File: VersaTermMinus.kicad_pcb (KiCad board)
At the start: 2 copper layers, 83.5 x 77.7 mm, 55 parts, among them CN1 HDMI_A, CN2 DE15_Socket, CN3 USB_B_Micro, CN5 USB_B_Micro, CN6 Mini-DIN-6, CN7 TTL Serial, CN8 DE9 Socket, J2 USBDATA, Q1 2N7002, Q2 2N7002, Q3 2N7002, Q4 2N7002, Q5 2N7002, Q6 2N7002, Q7 2N7002, SW1 RESET, SW2 DEFAULTS, SW3 3V3/5V, U1 Raspberry Pi Pico, U3 MAX3232

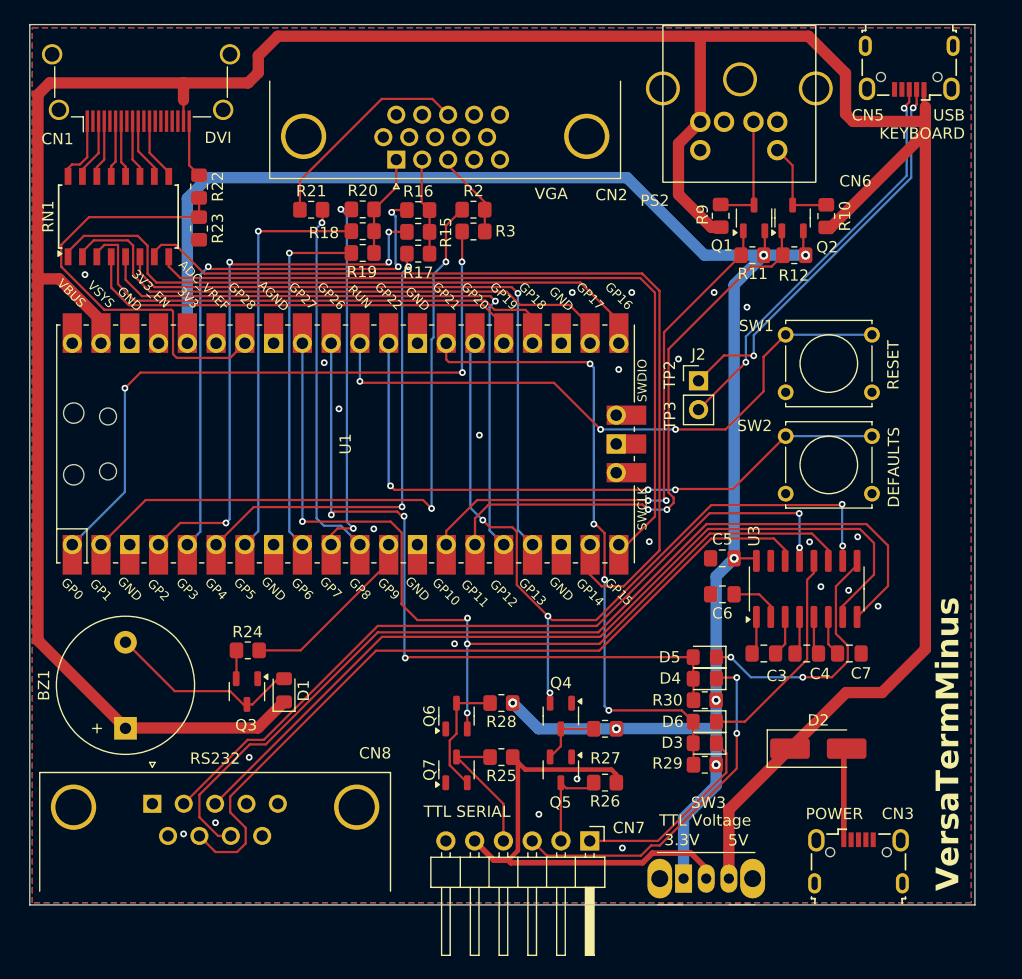
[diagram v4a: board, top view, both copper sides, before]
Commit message: fix incorrect schema symbols for 2n7002 transistors
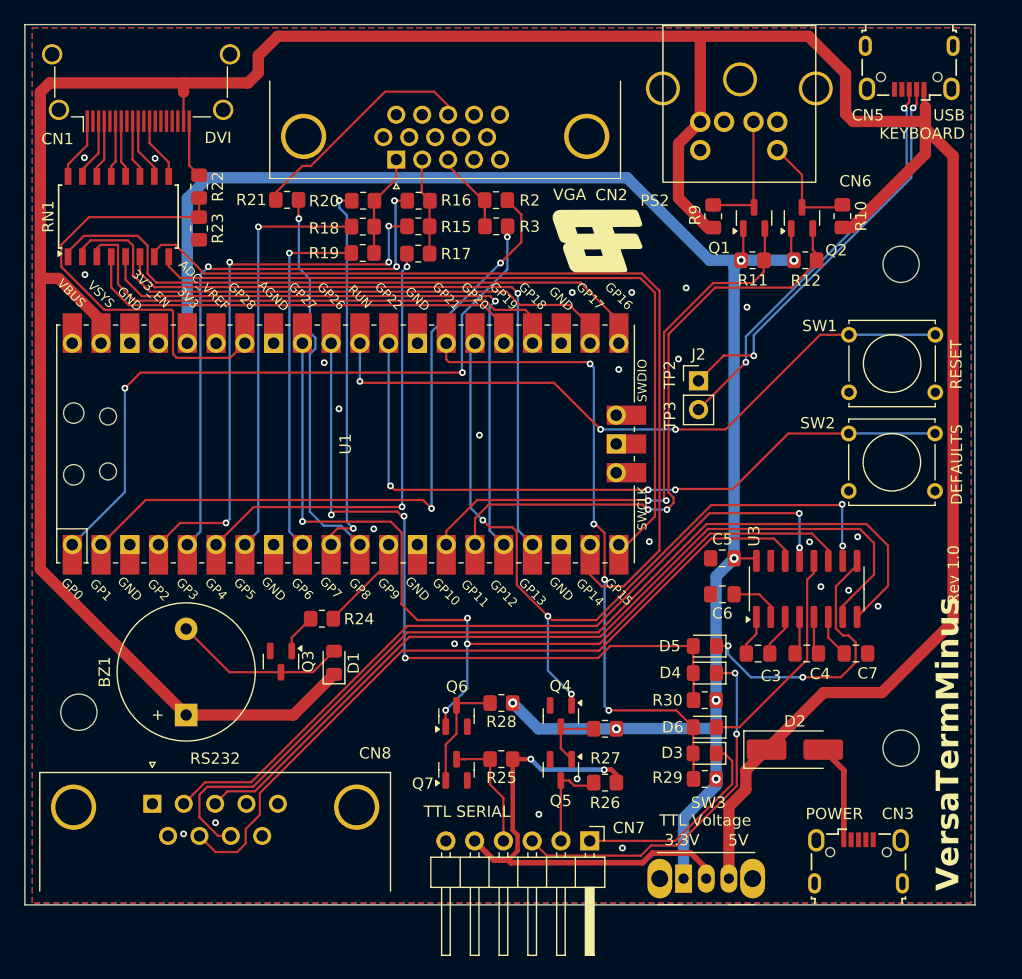
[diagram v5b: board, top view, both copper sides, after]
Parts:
- added G***: LOGO, Logos:BF, F.Cu at (108.3, 68.7)
- added G***: LOGO, Logos:tbs_logo, B.Cu at (123.7, 84.9)
- added G***: LOGO, Logos:mfmi_logo, B.Cu at (101.3, 88.3)
- added H1: MountingHole, MountingHole:MountingHole_3.2mm_M3, F.Cu at (135.1, 70.7)
- added H2: MountingHole, MountingHole:MountingHole_3.2mm_M3, F.Cu at (135.1, 113.4)
- added H3: MountingHole, MountingHole:MountingHole_3.2mm_M3, F.Cu at (62.5, 110.3)
- Q1, Q2, Q3, Q4, Q5, Q6, Q7: footprint Package_TO_SOT_SMD:SOT-23-3 -> Package_TO_SOT_SMD:SOT-23
- moved R24 7.12 mm to (84.0, 102.0)
- moved SW1 5.59 mm to (130.5, 76.9)
- moved SW2 5.57 mm to (130.5, 85.6)
- moved BZ1 5.49 mm to (72.0, 110.5)
- moved D1 5.04 mm to (85.1, 105.9)
- moved Q3 4.00 mm to (80.4, 105.8)
- moved R21 2.30 mm to (80.9, 65.0)
- moved R2 2.16 mm to (99.4, 65.0), turned to 180 degrees
- moved D2 2.07 mm to (125.8, 113.6)
- moved R3 2.07 mm to (99.4, 67.4), turned to 180 degrees
- moved R10 1.42 mm to (129.9, 66.5)
- moved R29 1.25 mm to (117.8, 116.2)
- moved R12 1.07 mm to (126.7, 70.4), turned to 180 degrees
- moved D5 0.98 mm to (117.8, 104.4)
- moved D3 0.89 mm to (117.8, 113.9)
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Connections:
- net Net-(CN2-Pad1) renamed /Red
- net Net-(CN2-Pad13) renamed /Sync
- net Net-(CN2-Pad2) renamed /Green
- net Net-(CN2-Pad3) renamed /Blue
- net Net-(Q1-D) renamed /Data
- net Net-(Q2-D) renamed /Clock
- Q1 pad 1: PS2DATA -> +3.3V
- Q1 pad 2: +3.3V -> PS2DATA
- Q2 pad 1: PS2CLK -> +3.3V
- Q2 pad 2: +3.3V -> PS2CLK
- Q3 pad 1: GND -> Net-(Q3-G)
- Q3 pad 2: Net-(Q3-G) -> GND
- Q4 pad 1: GND -> TXO
- Q4 pad 2: TXO -> GND
- Q5 pad 1: GND -> Net-(Q4-D)
- Q5 pad 2: Net-(Q4-D) -> GND
- Q6 pad 1: GND -> RTS
- Q6 pad 2: RTS -> GND
- Q7 pad 1: GND -> Net-(Q6-D)
- Q7 pad 2: Net-(Q6-D) -> GND
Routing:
- net BUZZ: track 16.2 -> 8.57 mm
- net DEFAULTS: track 57.3 -> 62.9 mm
- net PS2CLK: track 50.3 -> 54.7 mm
- net RESET: track 55.6 -> 59.4 mm
- net B1: track 58.6 -> 62.1 mm
- net +5V: track 283.5 -> 286.7 mm
- net PS2DATA: track 48.6 -> 51.4 mm
- net Net-(U3-T1OUT): track 69.5 -> 67.0 mm
- net CTSB: track 23.0 -> 25.2 mm
- net B0: track 58.6 -> 60.7 mm
- net Net-(BZ1--): track 17.2 -> 15.4 mm
- net SYNC: track 32.3 -> 34.0 mm
- net /Sync: track 19.2 -> 20.9 mm
- net Net-(CN7-Pin_4): track 12.1 -> 10.7 mm
- net CTS: track 63.7 -> 65.0 mm
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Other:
- board size 83.5 x 77.7 mm -> 83.9 x 77.7 mm
- board text added: "Rev 1.0"
- board text added: "https://www.youtube.com/@MoreFunMakingIt"

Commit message: version 1.1
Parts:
- CN5: value USB_B_Micro -> USB-A; footprint Connector_USB:USB_Micro-B_Wuerth_629105150521 -> Connector_USBA_Molex:CONN_67643-2911_MOL
- moved J2 39.5 mm to (78.0, 85.2)
- moved R10 13.8 mm to (116.2, 67.3)
- moved CN5 9.88 mm to (138.5, 62.9)
- moved R9 9.26 mm to (127.8, 67.3)
- moved R12 7.21 mm to (119.5, 71.0)
- moved Q2 6.95 mm to (119.5, 67.3)
- moved CN6 2.93 mm to (118.0, 56.8)
- moved Q1 2.21 mm to (124.3, 67.3)
- moved R11 2.21 mm to (124.1, 71.0)
- moved CN2 1.66 mm to (88.9, 61.5)
- moved CN1 0.28 mm to (67.7, 53.1)
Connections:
- CN5 pad 4: unconnected-(CN5-ID-Pad4) -> GND
- CN5 pad 6: GND -> (no net)
- CN6 pad 1: /Data -> unconnected-(CN6-Pad1)
- CN6 pad 2: unconnected-(CN6-Pad2) -> /Data
- CN6 pad 3: GND -> +5V
- CN6 pad 4: +5V -> GND
- CN6 pad 5: /Clock -> unconnected-(CN6-Pad5)
- CN6 pad 6: unconnected-(CN6-Pad6) -> /Clock
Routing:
- net Net-(CN5-D-): track 35.3 -> 70.8 mm, vias 2 -> 3
- net Net-(CN5-D+): track 36.2 -> 71.4 mm, vias 2 -> 3
- net +5V: track 286.7 -> 299.6 mm
- net G1: track 49.1 -> 59.0 mm
- net G0: track 48.9 -> 55.1 mm
- net PS2CLK: track 54.7 -> 49.0 mm
- net /Data: track 11.0 -> 14.9 mm
- net RESET: track 59.4 -> 55.6 mm
- net PS2DATA: track 51.4 -> 54.2 mm
- net +3.3V: track 153.4 -> 150.6 mm
- net /Sync: track 20.9 -> 18.7 mm
- net R0: track 36.8 -> 38.7 mm
- net /Blue: track 7.40 -> 8.85 mm
- net G2: track 40.5 -> 41.4 mm
- net /Red: track 9.06 -> 8.35 mm
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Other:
- board size 83.9 x 77.7 mm -> 86.2 x 78 mm
- board text added: "Rev 1.1"
- board text removed: "Rev 1.0"

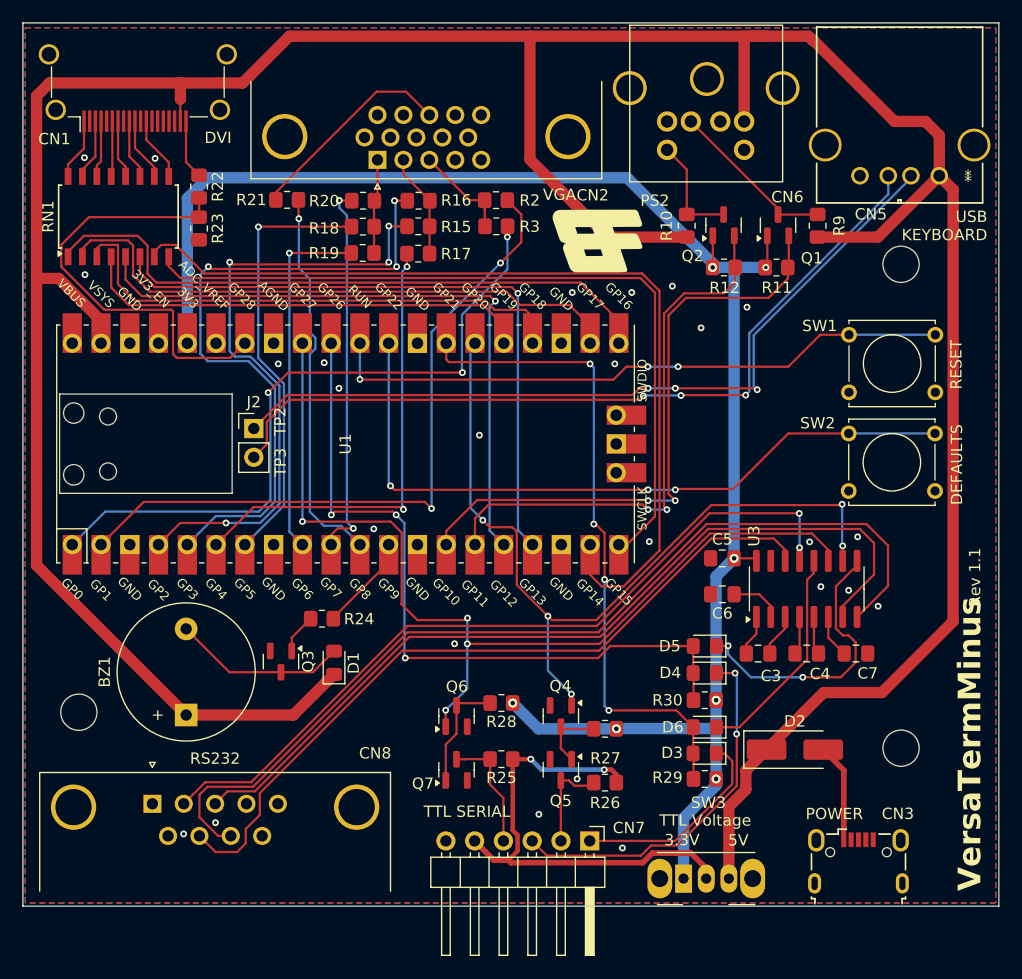
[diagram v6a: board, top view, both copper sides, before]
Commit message: add TP labels to back silkscreen
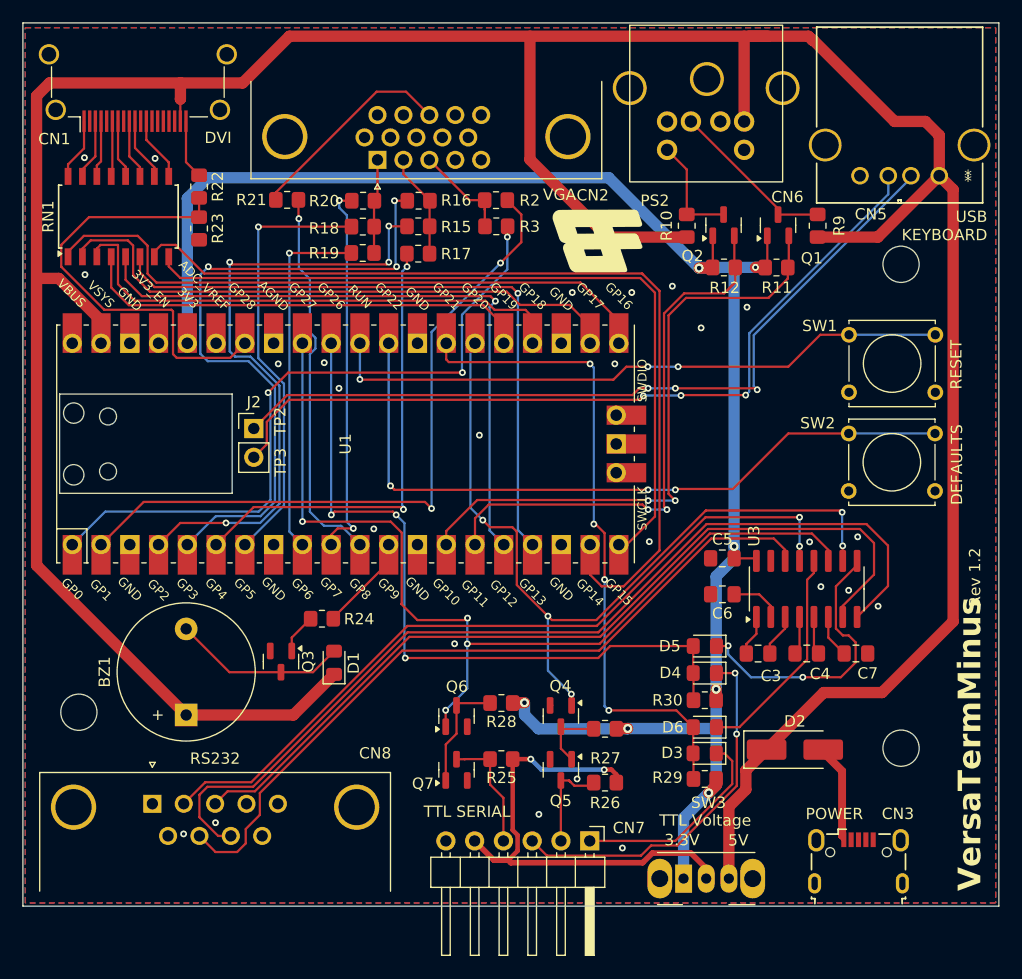
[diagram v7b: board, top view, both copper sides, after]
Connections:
- net Net-(CN3-VBUS) renamed /VBUS
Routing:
- net /VBUS: track 8.71 -> 17.4 mm
- net +3.3V: track 150.6 -> 157.7 mm
- net TXO: track 72.9 -> 72.1 mm
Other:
- board text added: "Rev 1.2"
- board text removed: "Rev 1.1"
